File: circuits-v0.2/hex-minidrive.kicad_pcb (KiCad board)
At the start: 2 copper layers, 30 x 30 mm, 14 parts

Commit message: Tentatively finish new schematic.
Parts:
- removed Q1: ~, Library:DFN-8_L3.3-W3.3-P0.65-BL-2
- removed Q2: ~, Library:DFN-8_L3.0-W3.0-P0.65-BL
- removed U2: ~, Library:QFN-16_L3.0-W3.0-P0.50-TL-EP1.7
- added C10: 10uF, Library:C1206, F.Cu at (97.8, 43.8)
- added C11: 10uF, Library:C1206, F.Cu at (97.8, 47.2)
- added C12: 1uF, Library:C0603, F.Cu at (107.0, 40.2)
- added C14: 10uF, Library:C1206, F.Cu at (97.8, 50.5)
- added C15: 10uF, Library:C1206, F.Cu at (97.8, 53.9)
- added C16: 10uF, Library:C1206, F.Cu at (97.8, 57.2)
- added C17: 10uF, Library:C1206, F.Cu at (97.8, 60.5)
- added C20: 15pF, Library:C0603, F.Cu at (107.0, 42.8)
- added C21: 15pF, Library:C0603, F.Cu at (107.0, 45.5)
- added C23: 1uF, Library:C0603, F.Cu at (107.0, 48.2)
- added C28: 10uF, Library:C1206, F.Cu at (97.8, 63.9)
- added C3: 10uF, Library:C1206, F.Cu at (97.8, 40.5)
- added C30: 1nF, Library:C0603, F.Cu at (111.0, 40.2)
- added C31: 1nF, Library:C0603, F.Cu at (111.0, 42.8)
- added C32: 1nF, Library:C0603, F.Cu at (111.0, 45.5)
- added C33: 1nF, Library:C0603, F.Cu at (111.0, 48.2)
- added C4: 22uF, Library:C0805, F.Cu at (97.2, 72.4)
- added C5: 22uF, Library:C0805, F.Cu at (97.2, 75.3)
- added C6: 100pF, Library:C0603, F.Cu at (102.9, 40.2)
- added C7: 1uF, Library:C0603, F.Cu at (102.9, 42.8)
- added C8: 1uF, Library:C0603, F.Cu at (102.9, 45.5)
- added C9: 10nF, Library:C0603, F.Cu at (102.9, 48.2)
- added D2: ~, Library:SOT-23-3_L3.0-W1.7-P0.95-LS2.9-BR, F.Cu at (115.2, 40.9)
- added L2: 10uH, Library:L0805, F.Cu at (114.1, 51.2)
- added L3: 300mΩ, Library:L0805, F.Cu at (114.1, 54.5)
- added LED1: ~, Library:LED-ARRAY-SMD_4P-L1.6-W1.5-BR_XL-1615RGBC-RF, F.Cu at (86.2, 74.8)
- added R10: 49.9Ω, Library:R0603, F.Cu at (80.9, 52.4)
- added R11: 1.5kΩ, Library:R0603, F.Cu at (80.9, 54.9)
- added R12: 1.5kΩ, Library:R0603, F.Cu at (80.9, 57.4)
- added R13: 1.5kΩ, Library:R0603, F.Cu at (84.9, 40.1)
- added R14: 10Ω, Library:R0603, F.Cu at (84.9, 42.5)
- added R15: 10Ω, Library:R0603, F.Cu at (84.9, 45.0)
- added R16: 10kΩ, Library:R0603, F.Cu at (84.9, 47.5)
- added R17: 100kΩ, Library:R0603, F.Cu at (84.9, 50.0)
- added R18: 10kΩ, Library:R0603, F.Cu at (84.9, 52.4)
- added R19: 10kΩ, Library:R0603, F.Cu at (84.9, 54.9)
- added R20: 10Ω, Library:R0603, F.Cu at (84.9, 57.4)
- added R21: 100kΩ, Library:R0603, F.Cu at (88.8, 40.1)
- added R22: 10Ω, Library:R0603, F.Cu at (88.8, 42.5)
- added R23: 10Ω, Library:R0603, F.Cu at (88.8, 45.0)
- added R24: 10Ω, Library:R0603, F.Cu at (88.8, 47.5)
- added R25: 5.1kΩ, Library:R0603, F.Cu at (88.8, 50.0)
- added R26: 10Ω, Library:R0603, F.Cu at (88.8, 52.4)
- added R27: 10Ω, Library:R0603, F.Cu at (88.8, 54.9)
- added R28: 100kΩ, Library:R0603, F.Cu at (88.8, 57.4)
- added R29: 10Ω, Library:R0603, F.Cu at (92.7, 40.1)
- added R30: 5.1kΩ, Library:R0603, F.Cu at (92.7, 42.5)
- added R31: 100kΩ, Library:R0603, F.Cu at (92.7, 45.0)
- added R33: 5.1kΩ, Library:R0603, F.Cu at (92.0, 48.0)
- added R5: 100kΩ, Library:R0603, F.Cu at (79.1, 40.0)
- added R6: 13kΩ, Library:R0603, F.Cu at (79.1, 41.4)
- added R7: 5.1kΩ, Library:R0603, F.Cu at (80.9, 45.0)
- added R8: 5.1kΩ, Library:R0603, F.Cu at (80.9, 47.5)
- added R9: 10Ω, Library:R0603, F.Cu at (80.9, 50.0)
- added U6: ~, Library:QFN-16_L3.0-W3.0-P0.50-TL-EP1.7, F.Cu at (110.2, 74.3)
- added U8: ~, Library:TSSOP-20_L6.5-W4.4-P0.65-LS6.4-BL, F.Cu at (111.5, 62.8)
- added X1: 16MHz, Library:OSC-SMD_4P-L3.2-W2.5-BL, F.Cu at (103.8, 74.1)
- D1: footprint Library:SMA_L4.3-W2.6-LS5.2-RD -> Library:SOD-123_L2.7-W1.6-LS3.7-RD-1
- moved U4 67.7 mm to (115.0, 73.9)
- moved U1 64.8 mm to (110.2, 69.5)
- moved U3 62.2 mm to (115.0, 69.4)
- moved USB1 56.5 mm to (106.3, 53.0)
- moved L1 50.1 mm to (97.6, 68.2)
- moved R1 48.3 mm to (104.0, 60.2), turned to 0 degrees
- moved R2 46.2 mm to (104.0, 63.6), turned to 0 degrees
- moved R3 44.5 mm to (104.0, 66.9), turned to 0 degrees
- moved R4 43.1 mm to (104.0, 70.2), turned to 0 degrees
- moved D1 31.2 mm to (81.8, 74.6)
- moved U5 18.4 mm to (86.2, 65.9)
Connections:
- D1 pad 1: unconnected-(D1-K-Pad1) -> 5V
- D1 pad 2: unconnected-(D1-A-Pad2) -> Net-(D1-+)
- L1 pad 1: unconnected-(L1-Pad1) -> Net-(U4-SW)
- L1 pad 2: unconnected-(L1-Pad2) -> 5V
- R1 pad 1: unconnected-(R1-Shunt-1-Pad1) -> Net-(Q1-S)
- R1 pad 2: unconnected-(R1-Shunt-2-Pad2) -> GND
- R1 pad 3: unconnected-(R1-Probe-1-Pad3) -> +Probe-1
- R1 pad 4: unconnected-(R1-Probe-2-Pad4) -> -Probe-1
- R2 pad 1: unconnected-(R2-Shunt-1-Pad1) -> Net-(Q3-S)
- R2 pad 2: unconnected-(R2-Shunt-2-Pad2) -> GND
- R2 pad 3: unconnected-(R2-Probe-1-Pad3) -> +Probe-2
- R2 pad 4: unconnected-(R2-Probe-2-Pad4) -> -Probe-2
- R3 pad 1: unconnected-(R3-Shunt-1-Pad1) -> Net-(Q5-S)
- R3 pad 2: unconnected-(R3-Shunt-2-Pad2) -> GND
- R3 pad 3: unconnected-(R3-Probe-1-Pad3) -> +Probe-3
- R3 pad 4: unconnected-(R3-Probe-2-Pad4) -> -Probe-3
- R4 pad 1: unconnected-(R4-Shunt-1-Pad1) -> Net-(Q7-S)
- R4 pad 2: unconnected-(R4-Shunt-2-Pad2) -> GND
- R4 pad 3: unconnected-(R4-Probe-1-Pad3) -> +Probe-4
- R4 pad 4: unconnected-(R4-Probe-2-Pad4) -> -Probe-4
- U1 pad 1: unconnected-(U1-HIN1-Pad1) -> TIM1_CH1
- U1 pad 10: unconnected-(U1-HO2-Pad10) -> P-Gate-2
- U1 pad 11: unconnected-(U1-LO2-Pad11) -> N-Gate-2
- U1 pad 14: unconnected-(U1-GND-Pad14) -> GND
- U1 pad 16: unconnected-(U1-HIN2-Pad16) -> TIM1_CH2
- U1 pad 3: unconnected-(U1-LIN2-Pad3) -> TIM1_CH2N
- U1 pad 4: unconnected-(U1-LIN1-Pad4) -> TIM1_CH1N
- U1 pad 6: unconnected-(U1-VCC1-Pad6) -> Net-(U1-VCC1)
- U1 pad 7: unconnected-(U1-VCC2-Pad7) -> VCC
- U1 pad 8: unconnected-(U1-HO1-Pad8) -> P-Gate-1
- U1 pad 9: unconnected-(U1-LO1-Pad9) -> N-Gate-1
- U3 pad 1: unconnected-(U3-IN-Pad1) -> 5V
- U3 pad 2: unconnected-(U3-GND-Pad2) -> GND
- U3 pad 3: unconnected-(U3-EN-Pad3) -> 5V
- U3 pad 4: unconnected-(U3-BYP-Pad4) -> Net-(U3-BYP)
- U3 pad 5: unconnected-(U3-OUT-Pad5) -> 3V3
- U4 pad 1: unconnected-(U4-GND-Pad1) -> GND
- U4 pad 2: unconnected-(U4-SW-Pad2) -> Net-(U4-SW)
- U4 pad 3: unconnected-(U4-VIN-Pad3) -> VCC
- U4 pad 4: unconnected-(U4-FB-Pad4) -> Buck-FB
- U4 pad 6: unconnected-(U4-BOOT-Pad6) -> Net-(U4-BOOT)
- U5 pad 16: unconnected-(U5-VDD-Pad16) -> 3V3
- U5 pad 32: unconnected-(U5-VDD-Pad32) -> 3V3
- U5 pad 48: unconnected-(U5-VDD-Pad48) -> 3V3
- U5 pad 5: unconnected-(U5-PF0-OSC_IN-Pad5) -> Net-(U5-PF0-OSC_IN)
- U5 pad 6: unconnected-(U5-PF1-OSC_OUT-Pad6) -> Net-(U5-PF1-OSC_OUT)
- U5 pad 64: unconnected-(U5-VDD-Pad64) -> 3V3
- USB1 pad A1B12: unconnected-(USB1-GND-PadA1B12) -> GND
- USB1 pad A4B9: unconnected-(USB1-VBUS-PadA4B9) -> USB:5V
- USB1 pad A5: unconnected-(USB1-CC1-PadA5) -> Net-(USB1-CC1)
- USB1 pad A6: unconnected-(USB1-DP1-PadA6) -> USB_D_P
- USB1 pad A7: unconnected-(USB1-DN1-PadA7) -> USB_D_N
- USB1 pad B1A12: unconnected-(USB1-GND-PadB1A12) -> GND
- USB1 pad B4A9: unconnected-(USB1-VBUS-PadB4A9) -> USB:5V
- USB1 pad B5: unconnected-(USB1-CC2-PadB5) -> Net-(USB1-CC2)
- USB1 pad B6: unconnected-(USB1-DP2-PadB6) -> USB_D_P
- USB1 pad B7: unconnected-(USB1-DN2-PadB7) -> USB_D_N

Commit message: Finish the new version schematic.
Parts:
- removed C17, C28: 10uF, Library:C1206
- removed C23: 1uF, Library:C0603
- removed C31, C32, C33: 1nF, Library:C0603
- removed R13: 1.5kΩ, Library:R0603
- removed R14, R15, R20, R24, R26, R27, R29, R9: 10Ω, Library:R0603
- removed R16, R19: 10kΩ, Library:R0603
- removed R25, R30, R33, R7, R8: 5.1kΩ, Library:R0603
- removed R28, R31: 100kΩ, Library:R0603
- added C1: 100nF, Library:C0603, F.Cu at (31.2, 26.5)
- added C101: 1nF, Library:C0603, F.Cu at (99.5, 56.0)
- added C13: 100nF, Library:C0603, F.Cu at (108.8, 84.0)
- added C2: 100nF, Library:C0603, F.Cu at (36.5, 18.5)
- added C201: 1nF, Library:C0603, F.Cu at (122.8, 64.0)
- added C24: 100nF, Library:C0603, F.Cu at (86.5, 134.0)
- added C25: 100nF, Library:C0603, F.Cu at (86.5, 119.0)
- added C26: 100nF, Library:C0603, F.Cu at (71.8, 119.5)
- added C27: 100nF, Library:C0603, F.Cu at (71.5, 131.5)
- added C301: 1nF, Library:C0603, F.Cu at (135.5, 63.0)
- added C34: 10nF, Library:C0603, F.Cu at (78.8, 134.0)
- added C401: 1nF, Library:C0603, F.Cu at (154.2, 61.5)
- added C501: 10uF, Library:C1206, F.Cu at (115.9, 34.1)
- added C502: 100nF, Library:C0603, F.Cu at (114.8, 37.1)
- added C601: 10uF, Library:C1206, F.Cu at (151.4, 33.1)
- added C602: 100nF, Library:C0603, F.Cu at (150.3, 36.1)
- added C801: 100nF, Library:C0603, F.Cu at (106.0, 67.7)
- added C802: 100nF, Library:C0603, F.Cu at (108.3, 74.1)
- added C803: 1uF, Library:C0603, F.Cu at (108.3, 76.8)
- added FPC1: ~, Library:FPC-SMD_6P-P0.50_XUNPU_FPC-05F-6PH20, F.Cu at (74.0, 54.0)
- added FPC2: ~, Library:FPC-SMD_6P-P0.50_XUNPU_FPC-05F-6PH20, F.Cu at (50.0, 52.1)
- added FPC3: ~, Library:FPC-SMD_6P-P0.50_XUNPU_FPC-05F-6PH20, F.Cu at (73.9, 45.5)
- added FPC4: ~, Library:FPC-SMD_20P-P0.50_XUNPU_FPC-05F-20PH20, F.Cu at (53.8, 45.5)
- added H1: 2.54mm 3P header, Library:HDR-TH_3P-P2.54-V-M-1, F.Cu at (76.5, 93.0)
- added H2: 2.54mm 3P header, Library:HDR-TH_3P-P2.54-V-M-1, F.Cu at (76.5, 101.0)
- added H3: 2.54mm 3P header, Library:HDR-TH_3P-P2.54-V-M-1, F.Cu at (47.5, 93.0)
- added H4: 2.54mm 3P header, Library:HDR-TH_3P-P2.54-V-M-1, F.Cu at (47.5, 101.0)
- added H5: 10P 1.27mm header, Library:HDR-TH_HX-PZ1.27-1X10P-ZZ, F.Cu at (55.5, 103.5)
- added P1: 2P 2.54mm header, Library:CONN-TH_2P-P2.50_XH-2AW, F.Cu at (70.8, 97.0)
- added Q1: ~, Library:DFN-8_L3.0-W3.0-P0.65-BL-MOSFET, F.Cu at (102.0, 50.6)
- added Q2: ~, Library:DFN-8_L3.0-W3.0-P0.65-BL-MOSFET, F.Cu at (103.3, 55.0)
- added Q3: ~, Library:DFN-8_L3.0-W3.0-P0.65-BL-MOSFET, F.Cu at (119.5, 51.0)
- added Q4: ~, Library:DFN-8_L3.0-W3.0-P0.65-BL-MOSFET, F.Cu at (119.5, 56.0)
- added Q5: ~, Library:DFN-8_L3.0-W3.0-P0.65-BL-MOSFET, F.Cu at (140.5, 50.2)
- added Q6: ~, Library:DFN-8_L3.0-W3.0-P0.65-BL-MOSFET, F.Cu at (140.5, 55.4)
- added Q7: ~, Library:DFN-8_L3.0-W3.0-P0.65-BL-MOSFET, F.Cu at (150.7, 54.1)
- added Q8: ~, Library:DFN-8_L3.0-W3.0-P0.65-BL-MOSFET, F.Cu at (150.7, 58.5)
- added R101: 10Ω, Library:R0603, F.Cu at (99.5, 50.0)
- added R102: 10Ω, Library:R0603, F.Cu at (105.5, 55.5)
- added R103: 100kΩ, Library:R0603, F.Cu at (99.5, 53.0)
- added R104: 5.1kΩ, Library:R0603, F.Cu at (101.0, 56.0)
- added R201: 10Ω, Library:R0603, F.Cu at (123.3, 54.0)
- added R202: 10Ω, Library:R0603, F.Cu at (123.3, 56.5)
- added R203: 100kΩ, Library:R0603, F.Cu at (123.3, 58.9)
- added R204: 5.1kΩ, Library:R0603, F.Cu at (123.3, 61.4)
- added R301: 10Ω, Library:R0603, F.Cu at (134.7, 54.0)
- added R302: 10Ω, Library:R0603, F.Cu at (135.0, 55.5)
- added R303: 100kΩ, Library:R0603, F.Cu at (135.2, 58.0)
- added R304: 5.1kΩ, Library:R0603, F.Cu at (135.0, 60.5)
- added R401: 10Ω, Library:R0603, F.Cu at (154.9, 51.6)
- added R402: 10Ω, Library:R0603, F.Cu at (154.9, 54.1)
- added R403: 100kΩ, Library:R0603, F.Cu at (154.9, 56.5)
- added R404: 5.1kΩ, Library:R0603, F.Cu at (154.9, 59.0)
- added R501: 10Ω, Library:R0603, F.Cu at (118.7, 37.0)
- added R601: 10Ω, Library:R0603, F.Cu at (154.2, 36.0)
- added R801: 10kΩ, Library:R0603, F.Cu at (112.2, 74.0)
- added R802: 10kΩ, Library:R0603, F.Cu at (112.2, 76.5)
- R11, R12: value 1.5kΩ -> 5.1kΩ
- R21: value 100kΩ -> 1.5kΩ
- R22, R23: value 10Ω -> 1.5kΩ
- U1: footprint Library:QFN-16_L3.0-W3.0-P0.50-TL-EP1.7 -> Library:LQFP-64_L10.0-W10.0-P0.50-LS12.0-BL
- U5: footprint Library:LQFP-64_L10.0-W10.0-P0.50-LS12.0-BL -> Library:QFN-16_L3.0-W3.0-P0.50-TL-EP1.7
- moved U4 103.2 mm to (31.0, 14.0)
- moved C20 97.2 mm to (61.5, 128.8)
- moved C21 93.2 mm to (61.7, 127.0)
- moved C30 91.5 mm to (20.8, 25.0)
- moved U3 87.3 mm to (35.0, 34.3)
- moved L1 80.0 mm to (31.5, 23.0)
- moved C5 79.5 mm to (36.5, 24.0)
- moved C4 78.9 mm to (36.5, 22.0), turned to 180 degrees
- moved C16 76.3 mm to (22.1, 48.0)
- moved C15 76.3 mm to (22.0, 45.5)
- moved C14 76.1 mm to (22.1, 43.0)
- moved C11 76.0 mm to (22.1, 40.5)
- moved C10 75.9 mm to (22.1, 38.0)
- moved C7 71.9 mm to (31.7, 33.0)
- moved C6 71.8 mm to (36.3, 13.5)
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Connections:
- C20 pad 2: Net-(U5-PF0-OSC_IN) -> Net-(U1-PF0-OSC_IN)
- C21 pad 2: Net-(U5-PF1-OSC_OUT) -> Net-(U1-PF1-OSC_OUT)
- C30 pad 2: ADC1_IN? -> ADC2_IN15/VOLTAGE
- R11 pad 1: unconnected-(R11-Pad1) -> GND
- R11 pad 2: Net-(LED1-R-) -> Net-(USB1-CC1)
- R12 pad 1: Net-(LED1-G-) -> GND
- R12 pad 2: unconnected-(R12-Pad2) -> Net-(USB1-CC2)
- R17 pad 1: ADC1_IN? -> ADC2_IN15/VOLTAGE
- R18 pad 2: ADC1_IN? -> ADC2_IN15/VOLTAGE
- R21 pad 1: ADC1_IN? -> TIM4_CH1/RED_LED
- R21 pad 2: M1 -> Net-(LED1-R-)
- R22 pad 1: Net-(Q4-G) -> Net-(LED1-G-)
- R22 pad 2: P-Gate-2 -> TIM4_CH2/GREEN_LED
- R23 pad 1: N-Gate-3 -> Net-(LED1-B-)
- R23 pad 2: Net-(Q5-G) -> TIM2_CH3/BLUE_LED
- U1 pad 1: TIM1_CH1 -> 3V3
- U1 pad 10: P-Gate-2 -> ADC1_IN8/POT_2
- U1 pad 11: N-Gate-2 -> TIM1_CH4
- U1 pad 12: unconnected-(U1-HO3-Pad12) -> ADC1_IN1/M1_CURRENT
- U1 pad 13: unconnected-(U1-LO3-Pad13) -> OPAMP1_VINP/M1_VOLTAGE
- U1 pad 14: GND -> ADC1_IN3/HALF_3V3_REF
- U1 pad 15: unconnected-(U1-HIN3-Pad15) -> GND
- U1 pad 16: TIM1_CH2 -> 3V3
- U1 pad 17: unconnected-(U1-EP-Pad17) -> ADC1_IN3/HALF_3V3_REF
- U1 pad 2: unconnected-(U1-LIN3-Pad2) -> TIM1_CH1N
- U1 pad 3: TIM1_CH2N -> FREE_IO_1
- U1 pad 4: TIM1_CH1N -> FREE_IO_2
- U1 pad 5: unconnected-(U1-5V-Pad5) -> Net-(U1-PF0-OSC_IN)
- U1 pad 6: Net-(U1-VCC1) -> Net-(U1-PF1-OSC_OUT)
- U1 pad 7: VCC -> NRST
- U1 pad 8: P-Gate-1 -> TIM1_CH1
- U1 pad 9: N-Gate-1 -> ADC1_IN7/POT_1
- U5 pad 1: unconnected-(U5-VBAT-Pad1) -> TIM1_CH1
- U5 pad 10: unconnected-(U5-PC2-Pad10) -> P-Gate-2
- U5 pad 11: unconnected-(U5-PC3-Pad11) -> N-Gate-2
- U5 pad 14: unconnected-(U5-PA2-Pad14) -> GND
- U5 pad 15: unconnected-(U5-VSS-Pad15) -> GND
- U5 pad 16: 3V3 -> TIM1_CH2
- U5 pad 2: unconnected-(U5-PC13-Pad2) -> GND
- U5 pad 3: unconnected-(U5-PC14-OSC32_IN-Pad3) -> TIM1_CH2N
- U5 pad 4: unconnected-(U5-PC15-OSC32_OUT-Pad4) -> TIM1_CH1N
- U5 pad 5: Net-(U5-PF0-OSC_IN) -> unconnected-(U5-5V-Pad5)
- U5 pad 6: Net-(U5-PF1-OSC_OUT) -> Net-(U5-VCC1)
- U5 pad 7: unconnected-(U5-PG10-NRST-Pad7) -> VCC
- U5 pad 8: unconnected-(U5-PC0-Pad8) -> P-Gate-1
- U5 pad 9: unconnected-(U5-PC1-Pad9) -> N-Gate-1
- U6 pad 15: unconnected-(U6-HIN3-Pad15) -> GND
- U6 pad 2: unconnected-(U6-LIN3-Pad2) -> GND
- U8 pad 1: ADC1_IN5/REF -> ADC1_IN3/HALF_3V3_REF
- U8 pad 12: ADC1_IN5/REF -> ADC1_IN3/HALF_3V3_REF
- U8 pad 13: unconnected-(U8-OUT3-Pad13) -> ADC1_IN12/M3_CURRENT
- U8 pad 19: unconnected-(U8-OUT4-Pad19) -> ADC2_IN14/M4_CURRENT
- U8 pad 2: unconnected-(U8-OUT1-Pad2) -> ADC1_IN1/M1_CURRENT
- U8 pad 20: ADC1_IN5/REF -> ADC1_IN3/HALF_3V3_REF
- U8 pad 8: unconnected-(U8-OUT2-Pad8) -> ADC2_IN3/M2_CURRENT
- U8 pad 9: ADC1_IN5/REF -> ADC1_IN3/HALF_3V3_REF
- X1 pad 1: Net-(U5-PF0-OSC_IN) -> Net-(U1-PF0-OSC_IN)
- X1 pad 3: Net-(U5-PF1-OSC_OUT) -> Net-(U1-PF1-OSC_OUT)
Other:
- board size 30 x 30 mm -> 32 x 64 mm

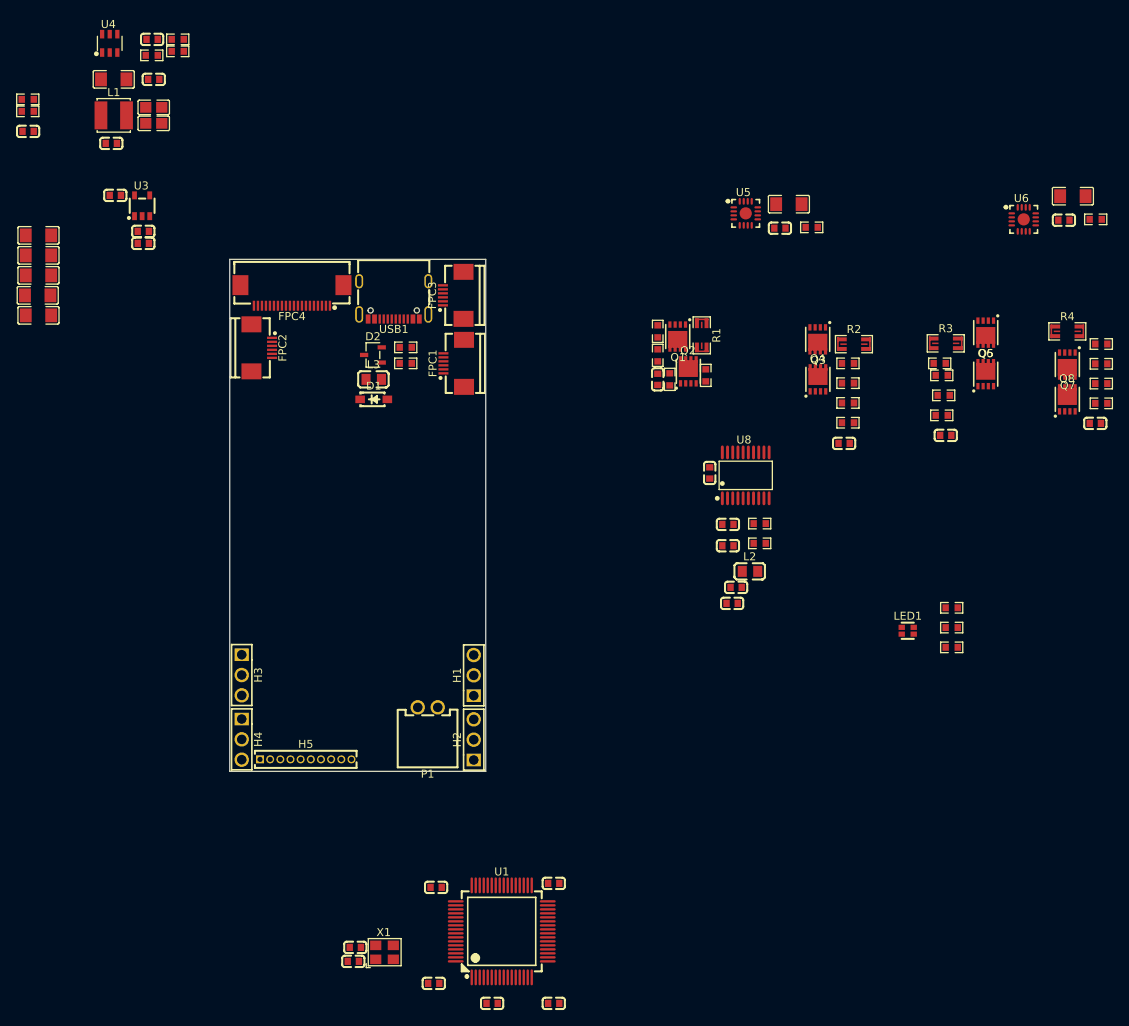
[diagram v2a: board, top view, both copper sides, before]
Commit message: Update electrical design rules.
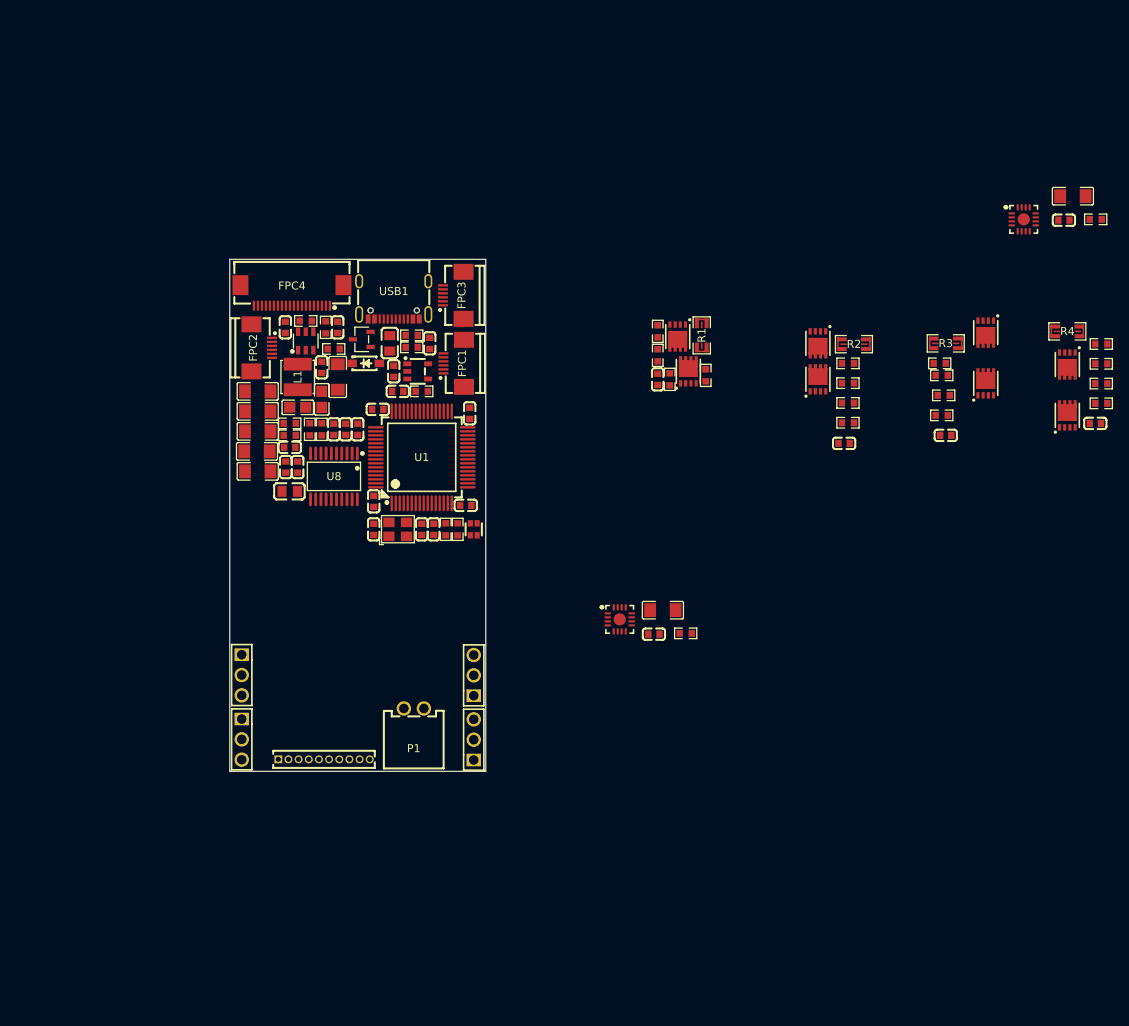
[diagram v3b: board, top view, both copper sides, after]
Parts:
- moved R23 73.6 mm to (70.0, 57.5)
- moved R22 64.4 mm to (73.0, 74.8), turned to 90 degrees
- moved C24 63.2 mm to (75.5, 71.8), turned to 180 degrees
- moved R21 62.5 mm to (74.5, 74.8), turned to 90 degrees
- moved C27 60.7 mm to (64.0, 71.2), turned to -90 degrees
- moved C26 60.2 mm to (64.5, 59.8)
- moved U1 60.1 mm to (70.0, 65.8)
- moved C34 59.7 mm to (71.5, 74.8), turned to 90 degrees
- moved C25 59.7 mm to (76.0, 60.2), turned to -90 degrees
- moved L2 58.4 mm to (53.5, 70.0)
- moved C13 58.3 mm to (53.0, 67.0), turned to -90 degrees
- moved R802 58.0 mm to (56.0, 62.2), turned to -90 degrees
- moved C12 56.8 mm to (54.5, 67.0), turned to -90 degrees
- moved R801 56.0 mm to (57.5, 62.2), turned to 90 degrees
- moved LED1 55.7 mm to (76.5, 74.8), turned to 90 degrees
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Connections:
- net Net-(C6-Pad2) renamed /Buck-Probe-Point
- net Net-(LED1-B-) renamed /Blue-LED
- net Net-(LED1-G-) renamed /Green-LED
- net Net-(LED1-R-) renamed /Red-LED
- net Net-(Q1-G) renamed /Gate-1-Negative
- net Net-(Q1-S) renamed /Shunt-1
- net Net-(Q2-G) renamed /Gate-1-Positive
- net Net-(Q3-G) renamed /Gate-2-Negative
- net Net-(Q3-S) renamed /Shunt-2
- net Net-(Q4-G) renamed /Gate-2-Positive
- net Net-(Q5-G) renamed /Gate-3-Negative
- net Net-(Q5-S) renamed /Shunt-3
- net Net-(Q6-G) renamed /Gate-3-Positive
- net Net-(Q7-G) renamed /Gate-4-Negative
- net Net-(Q7-S) renamed /Shunt-4
- net Net-(Q8-G) renamed /Gate-4-Positive
- net Net-(U3-BYP) renamed /LDO-Bypass-Capacitor
- net Net-(U4-BOOT) renamed /Buck-Bootstrap-Capacitor
- net Net-(U4-SW) renamed /Buck-Output-SW
